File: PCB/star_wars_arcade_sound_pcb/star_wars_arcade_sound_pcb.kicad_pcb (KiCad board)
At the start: 2 copper layers, 292.1 x 227.3 mm, 162 parts, among them P1 sw_main_connector, P2 sw_aud_connector, P3 sw_audio_edge_connector, Q1 2N3906, Q2 2N3906, Q3 2N3904, Q4 2N3904

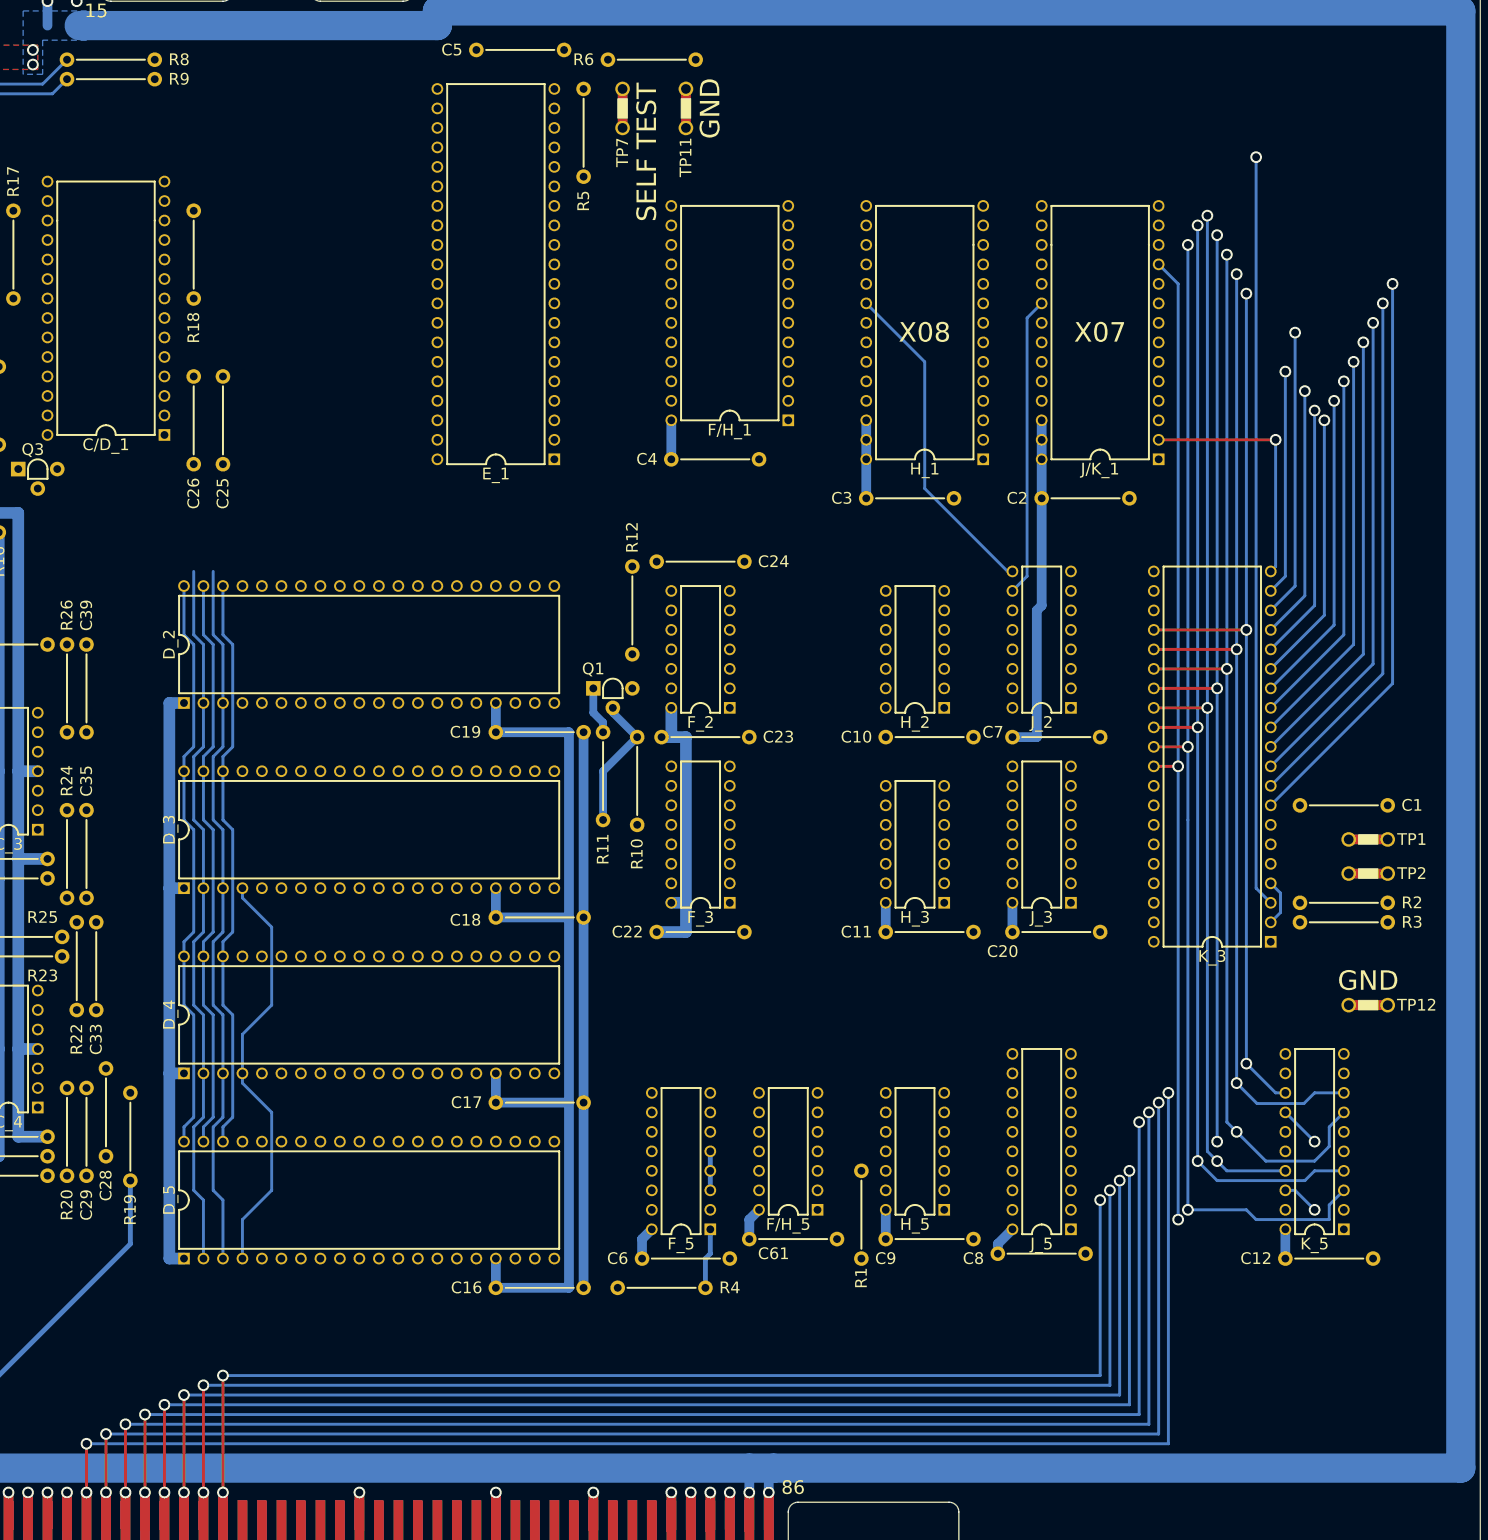
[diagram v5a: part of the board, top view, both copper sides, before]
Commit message: 374 connections remain
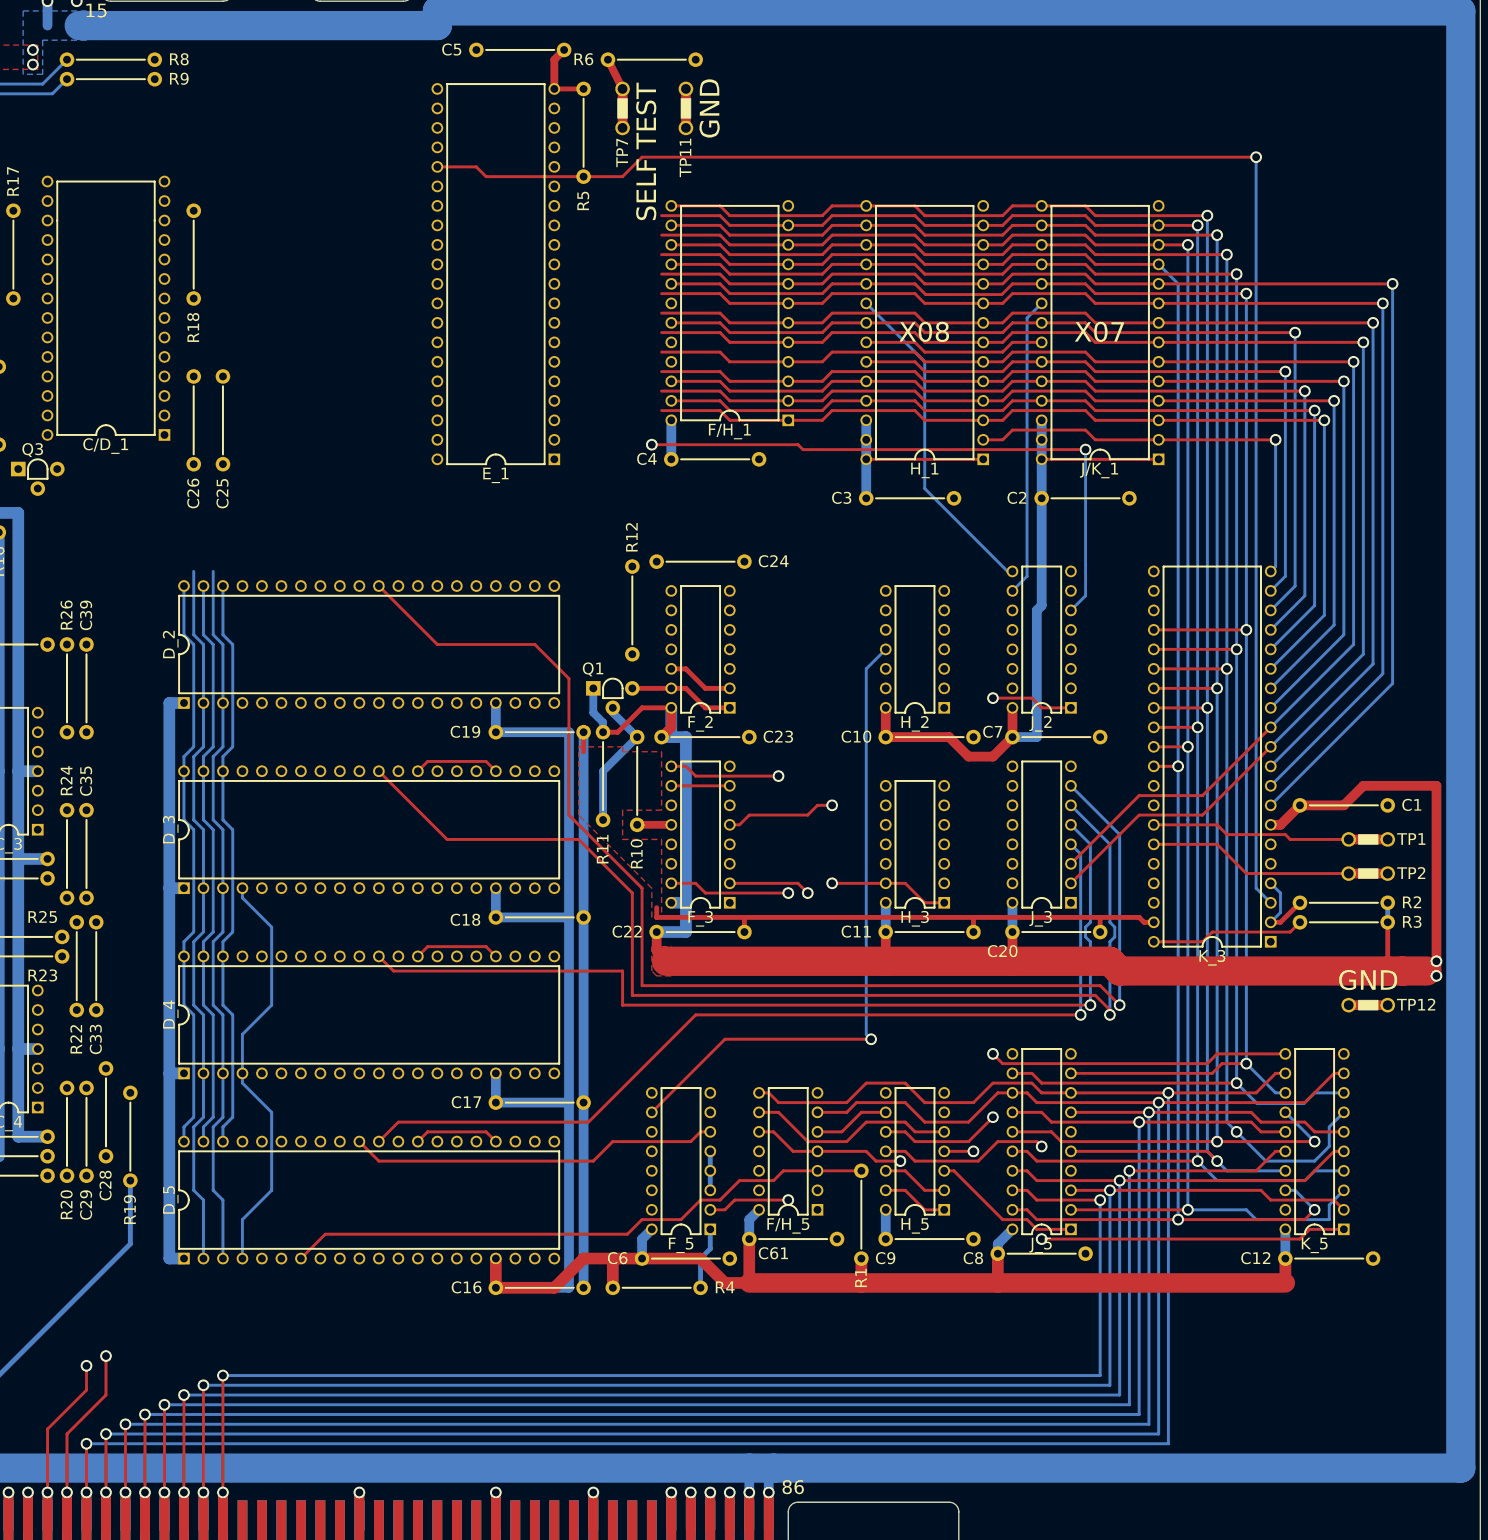
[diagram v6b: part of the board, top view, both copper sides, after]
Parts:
- moved R4 0.63 mm to (216.5, 223.5)
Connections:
- J_3 pad 4: ~{CIO}3 -> ~{CIO}0
- J_3 pad 5: ~{CIO}2 -> ~{CIO}1
- J_3 pad 6: ~{CIO}1 -> ~{CIO}2
- J_3 pad 7: ~{CIO}0 -> ~{CIO}3
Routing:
- net +5V: track 1330.0 -> 1706.6 mm, vias 10 -> 12
- net ~{CIO}3: track 0.00 -> 168.2 mm, vias 0 -> 1
- net ~{CIO}2: track 0.00 -> 146.5 mm, vias 0 -> 1
- net SA3: track 57.7 -> 185.2 mm
- net SA4: track 52.1 -> 178.3 mm
- net ~{CIO}1: track 0.00 -> 123.0 mm, vias 0 -> 1
- net ~{CIO}0: track 0.00 -> 121.0 mm, vias 0 -> 1
- net PHI_E: track 5.08 -> 124.7 mm, vias 0 -> 1
- net SD4: track 225.0 -> 338.6 mm
- net ~{SIRQ}: track 97.9 -> 206.2 mm
- net SD0: track 209.1 -> 316.9 mm
- net GND: track 243.0 -> 350.2 mm
- net SD6: track 131.9 -> 237.9 mm
- net SD7: track 119.1 -> 220.1 mm
- net SA0: track 74.5 -> 172.4 mm
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- added copper zone on F.Cu, net GND

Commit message: 331 connections remain
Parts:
- moved R9 1.42 mm to (146.1, 64.8)
- moved R8 1.42 mm to (146.1, 62.2)
- moved C5 0.63 mm to (198.8, 61.6)
- moved Q3 0.63 mm to (135.9, 117.5)
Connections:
- Q2 pad 1: Net-(Q2-Pad1) -> +5V
- R14 pad 2: Net-(Q2-Pad1) -> +5V
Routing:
- net PA3: track 0.00 -> 194.6 mm, vias 0 -> 2
- net +5V: track 1706.6 -> 1882.5 mm
- net -5V: track 229.9 -> 348.8 mm
- net SA0: track 172.4 -> 286.0 mm, vias 1 -> 3
- net SD3: track 325.4 -> 428.2 mm, vias 3 -> 4
- net SD2: track 320.9 -> 417.5 mm, vias 3 -> 5
- net SD4: track 338.6 -> 433.0 mm, vias 4 -> 6
- net PB4: track 0.00 -> 89.7 mm, vias 0 -> 1
- net SD0: track 316.9 -> 401.8 mm, vias 3 -> 5
- net PA5: track 0.00 -> 83.4 mm
- net SD1: track 315.7 -> 398.9 mm, vias 3 -> 6
- net SA1: track 165.5 -> 248.3 mm, vias 1 -> 3
- net PB1: track 0.00 -> 82.0 mm, vias 0 -> 1
- net PA1: track 0.00 -> 81.2 mm
- net PB2: track 0.00 -> 79.5 mm, vias 0 -> 1
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
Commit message: 285 connections remain
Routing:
- net PD0: track 174.0 -> 198.7 mm
- net SD5: track 312.2 -> 333.8 mm
- net P: track 110.0 -> 127.4 mm
- net Net-(C32-Pad2): track 0.00 -> 15.9 mm
- net Net-(C48-Pad1): track 0.00 -> 14.0 mm
- net ~{MAINREAD}: track 62.1 -> 74.1 mm
- net Net-(B_2-Pad7): track 5.08 -> 15.9 mm
- net Net-(B_3-Pad6): track 0.00 -> 9.72 mm
- net Net-(B_2-Pad1): track 0.00 -> 8.26 mm
- net AUD: track 5.08 -> 12.7 mm
- net PD3: track 198.7 -> 206.3 mm
- net Net-(DS1-Pad2): track 0.00 -> 6.35 mm
- net Net-(B_2-Pad10): track 0.00 -> 5.72 mm
- net Net-(B_2-Pad9): track 0.00 -> 5.71 mm
- net Net-(B_2-Pad3): track 0.00 -> 5.71 mm
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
